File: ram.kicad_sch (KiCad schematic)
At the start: 18 parts, among them U19 HM62256BLP, U20 74LS245

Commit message: chore: sync files
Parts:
- D49, D50, D51, D52, D53, D54, D55, D56: footprint (none) -> LED_SMD:LED_0805_2012Metric
- R49, R50, R51, R52, R53, R54, R55, R56: footprint (none) -> Resistor_SMD:R_0805_2012Metric
- U19: footprint Package_DIP:DIP-28_W15.24mm -> Package_DIP:DIP-28_W15.24mm_Socket
- U20: footprint (none) -> Package_DIP:DIP-20_W7.62mm_Socket
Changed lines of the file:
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@@
 			)
 		)
-		(property "Footprint" "Package_DIP:DIP-28_W15.24mm"
+		(property "Footprint" "Package_DIP:DIP-28_W15.24mm_Socket"
 			(at 99.06 100.33 0)
 			(hide yes)
@@
 			)
 		)
-		(property "Footprint" ""
+		(property "Footprint" "LED_SMD:LED_0805_2012Metric"
 			(at 151.13 119.38 0)
 			(hide yes)
@@
 			)
 		)
-		(property "Footprint" ""
+		(property "Footprint" "LED_SMD:LED_0805_2012Metric"
 			(at 135.89 119.38 0)
 			(hide yes)
@@
 			)
 		)
-		(property "Footprint" ""
+		(property "Footprint" "Resistor_SMD:R_0805_2012Metric"
 			(at 134.112 111.76 90)
 			(hide yes)
@@
 			)
 		)
-		(property "Footprint" ""
+		(property "Footprint" "LED_SMD:LED_0805_2012Metric"
 			(at 156.21 119.38 0)
 			(hide yes)
@@
 			)
 		)
-		(property "Footprint" ""
+		(property "Footprint" "Package_DIP:DIP-20_W7.62mm_Socket"
 			(at 201.93 92.71 0)
 			(hide yes)
@@
 			)
 		)
-		(property "Footprint" ""
+		(property "Footprint" "Resistor_SMD:R_0805_2012Metric"
 			(at 154.432 111.76 90)
 			(hide yes)
@@
 			)
 		)
-		(property "Footprint" ""
+		(property "Footprint" "LED_SMD:LED_0805_2012Metric"
 			(at 161.29 119.38 0)
 			(hide yes)
@@
 			)
 		)
-		(property "Footprint" ""
+		(property "Footprint" "Resistor_SMD:R_0805_2012Metric"
 			(at 159.512 111.76 90)
 			(hide yes)
@@
 			)
 		)
-		(property "Footprint" ""
+		(property "Footprint" "LED_SMD:LED_0805_2012Metric"
 			(at 140.97 119.38 0)
 			(hide yes)
@@
 			)
 		)
-		(property "Footprint" ""
+		(property "Footprint" "LED_SMD:LED_0805_2012Metric"
 			(at 130.81 119.38 0)
 			(hide yes)
@@
 			)
 		)
-		(property "Footprint" ""
+		(property "Footprint" "Resistor_SMD:R_0805_2012Metric"
 			(at 164.592 111.76 90)
 			(hide yes)
@@
 			)
 		)
-		(property "Footprint" ""
+		(property "Footprint" "LED_SMD:LED_0805_2012Metric"
 			(at 146.05 119.38 0)
 			(hide yes)
@@
 			)
 		)
-		(property "Footprint" ""
+		(property "Footprint" "Resistor_SMD:R_0805_2012Metric"
 			(at 149.352 111.76 90)
 			(hide yes)
@@
 			)
 		)
-		(property "Footprint" ""
+		(property "Footprint" "Resistor_SMD:R_0805_2012Metric"
 			(at 144.272 111.76 90)
 			(hide yes)
@@
 			)
 		)
-		(property "Footprint" ""
+		(property "Footprint" "Resistor_SMD:R_0805_2012Metric"
 			(at 129.032 111.76 90)
 			(hide yes)
@@
 			)
 		)
-		(property "Footprint" ""
+		(property "Footprint" "LED_SMD:LED_0805_2012Metric"
 			(at 166.37 119.38 0)
 			(hide yes)
@@
 			)
 		)
-		(property "Footprint" ""
+		(property "Footprint" "Resistor_SMD:R_0805_2012Metric"
 			(at 139.192 111.76 90)
 			(hide yes)

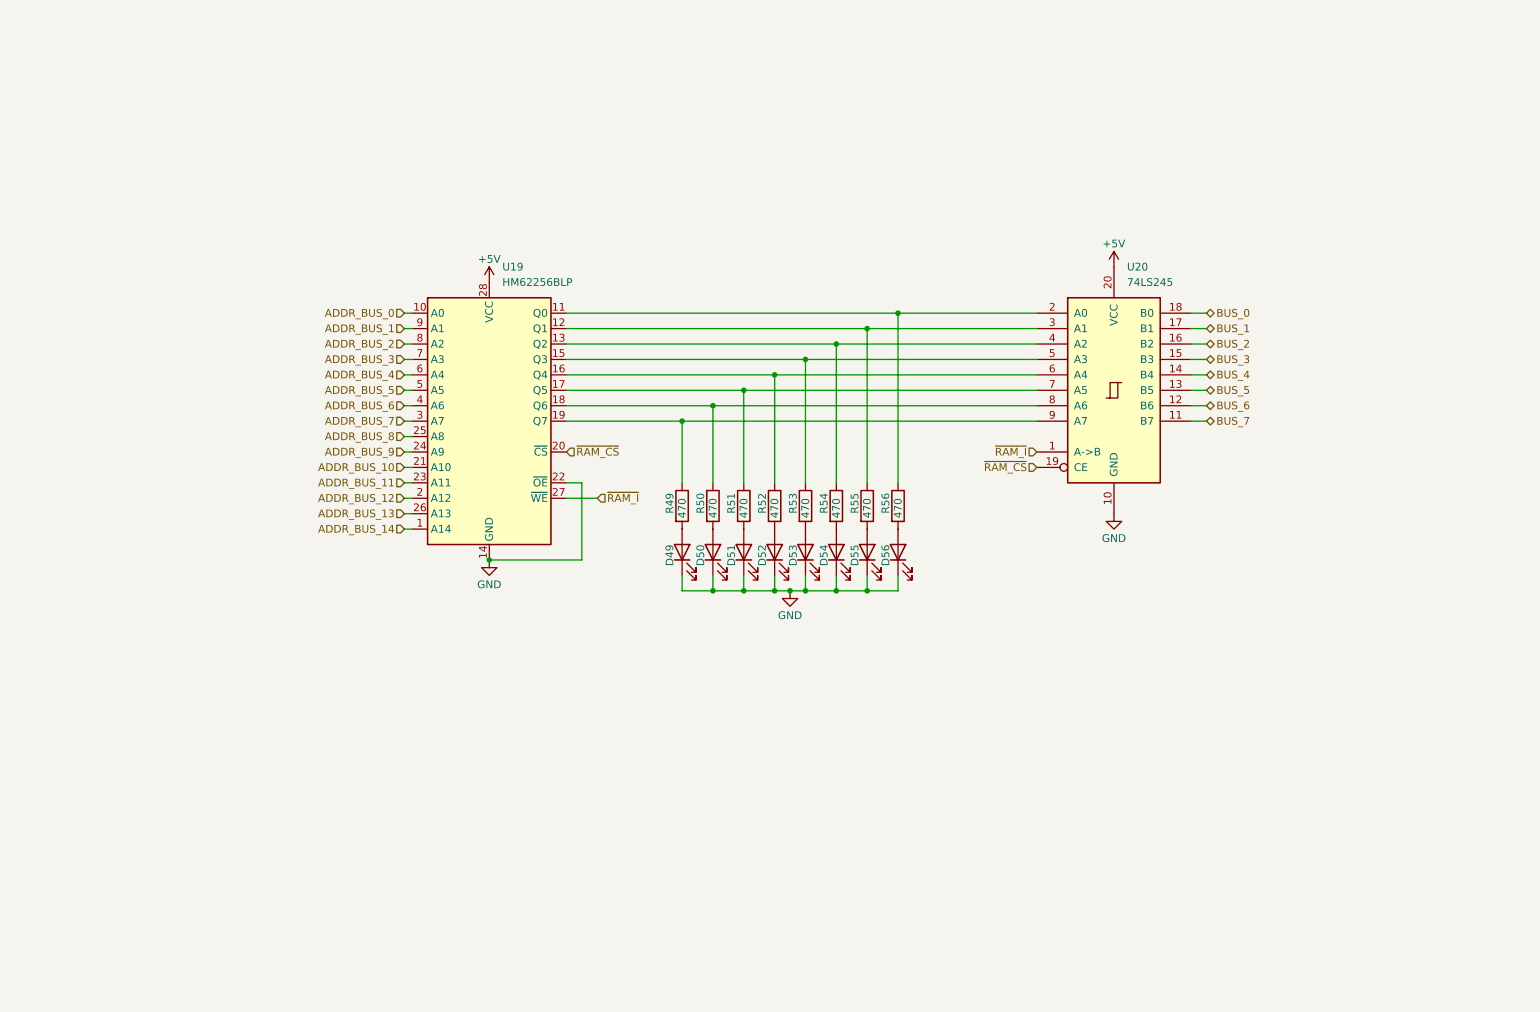
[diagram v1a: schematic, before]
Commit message: chore: sync design between simulation and schematic
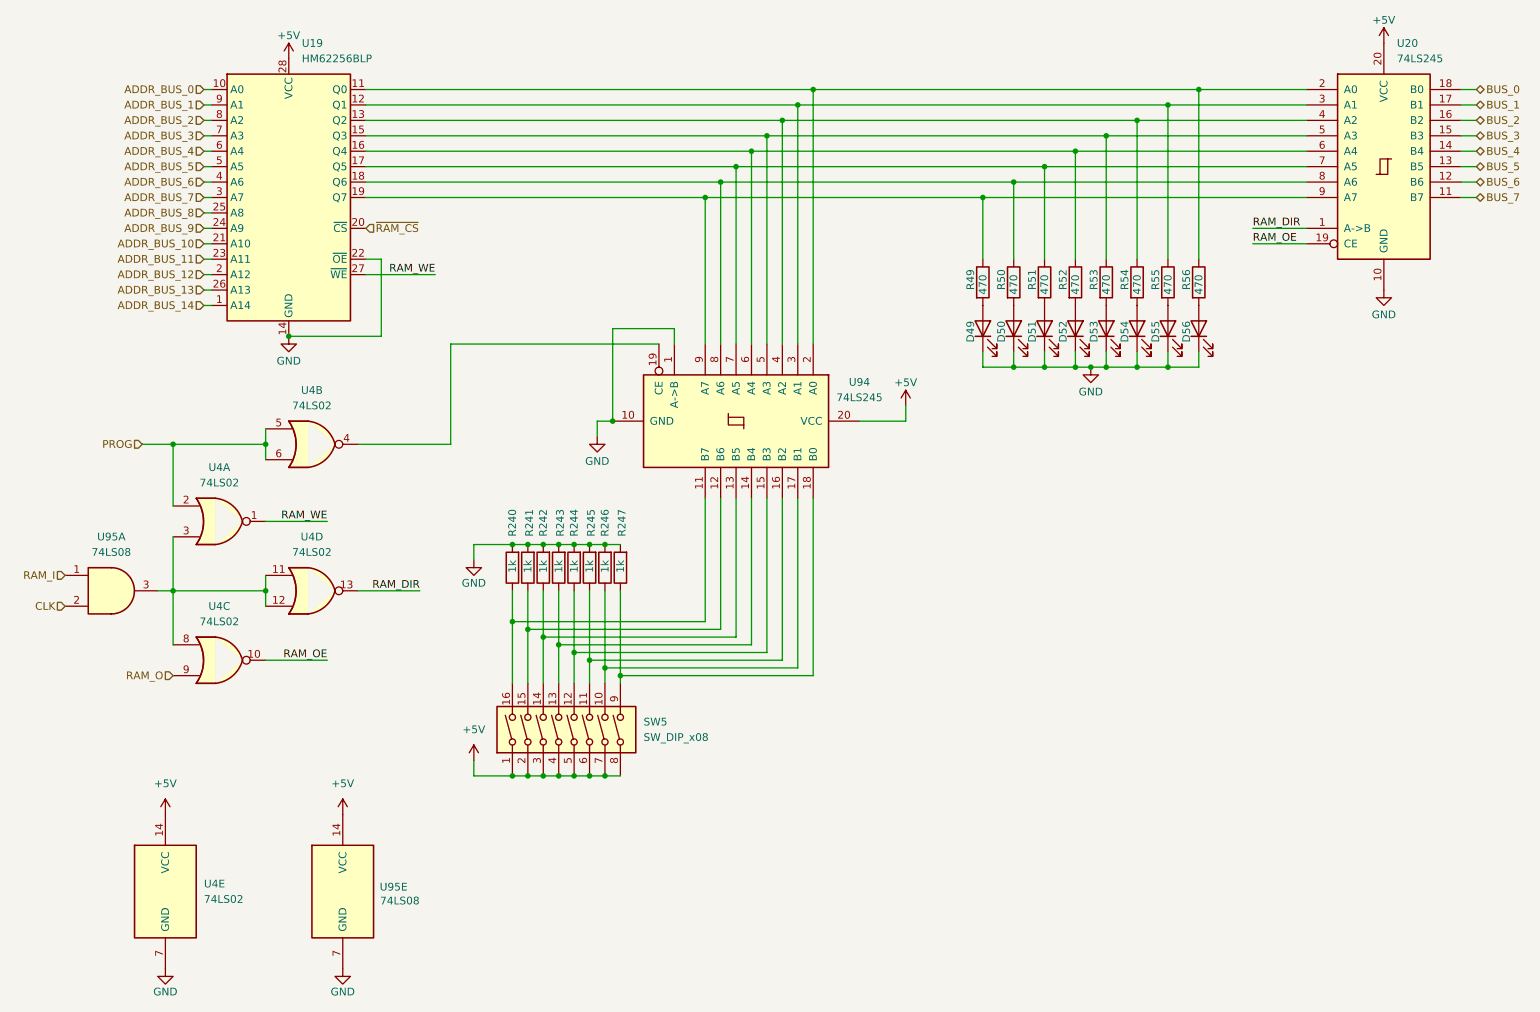
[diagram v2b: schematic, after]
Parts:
- added R240, R241, R242, R243, R244, R245, R246, R247: 1k, Resistor_SMD:R_0805_2012Metric, symbol Device:R
- added SW5: SW_DIP_x08, symbol Switch:SW_DIP_x08
- added U4: 74LS02, symbol 74xx:74LS02
- added U94: 74LS245, Package_DIP:DIP-20_W7.62mm_Socket, symbol 74xx:74LS245
- added U95: 74LS08, symbol 74xx:74LS08
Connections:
- net +5V: now also SW5.1, SW5.2, SW5.3, SW5.4, SW5.5, SW5.6, SW5.7, SW5.8, U4.14 (VCC), U94.20 (VCC), U95.14 (VCC)
- net GND: now also R240.2, R241.2, R242.2, R243.2, R244.2, R245.2, R246.2, R247.2, U4.7 (GND), U94.1 (A->B), U94.10 (GND), U95.7 (GND)
- net ~{RAM_CS}: no longer U20.19 (CE)
- net at R56.1, U19.11 (Q0), U20.2 (A0): now also U94.2 (A0)
- net at R55.1, U19.12 (Q1), U20.3 (A1): now also U94.3 (A1)
- net at R54.1, U19.13 (Q2), U20.4 (A2): now also U94.4 (A2)
- net at R53.1, U19.15 (Q3), U20.5 (A3): now also U94.5 (A3)
- net at R52.1, U19.16 (Q4), U20.6 (A4): now also U94.6 (A4)
- net at R51.1, U19.17 (Q5), U20.7 (A5): now also U94.7 (A5)
- net at R50.1, U19.18 (Q6), U20.8 (A6): now also U94.8 (A6)
- net at R49.1, U19.19 (Q7), U20.9 (A7): now also U94.9 (A7)
- net ~{RAM_I} renamed RAM_DIR
- net RAM_DIR: now also U4.13; no longer U19.27 (~{WE})
- new net: U4.11, U4.12, U4.3, U4.8, U95.3
- new net: R240.1, SW5.16, U94.11 (B7)
- new net: R246.1, SW5.10, U94.17 (B1)
- new net: R245.1, SW5.11, U94.16 (B2)
- new net: R244.1, SW5.12, U94.15 (B3)
- new net: R243.1, SW5.13, U94.14 (B4)
- new net: R242.1, SW5.14, U94.13 (B5)
- new net: R241.1, SW5.15, U94.12 (B6)
- new net: R247.1, SW5.9, U94.18 (B0)
- new net: U4.4, U94.19 (CE)
- new net CLK: U95.2
- new net PROG: U4.2, U4.5, U4.6
- new net RAM_I: U95.1
- new net RAM_O: U4.9
- new net RAM_OE: U20.19 (CE), U4.10
- new net RAM_WE: U19.27 (~{WE}), U4.1
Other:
- moved on the sheet: D49, D50, D51, D52, D53, D54, D55, D56, R49, R50, R51, R52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
